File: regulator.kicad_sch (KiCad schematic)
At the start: 20 parts, among them U3 LMR51635, U4 INA180A2

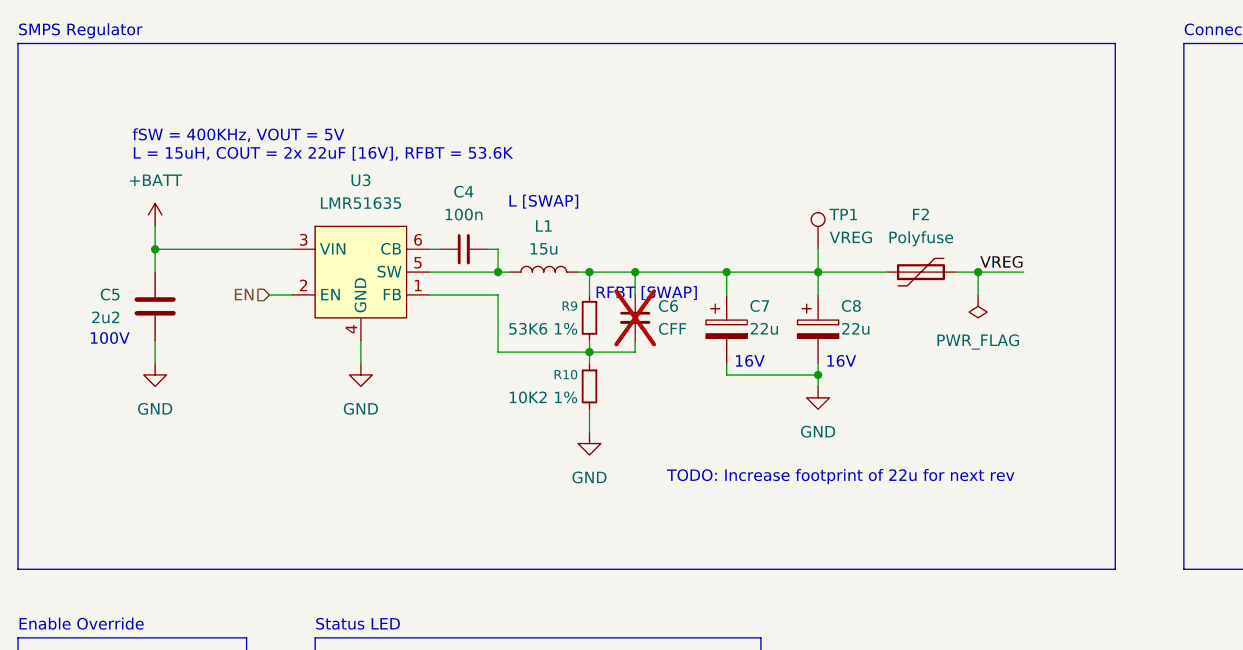
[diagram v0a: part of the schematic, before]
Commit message: fix capacitor sizes, clean up silkscreen, export
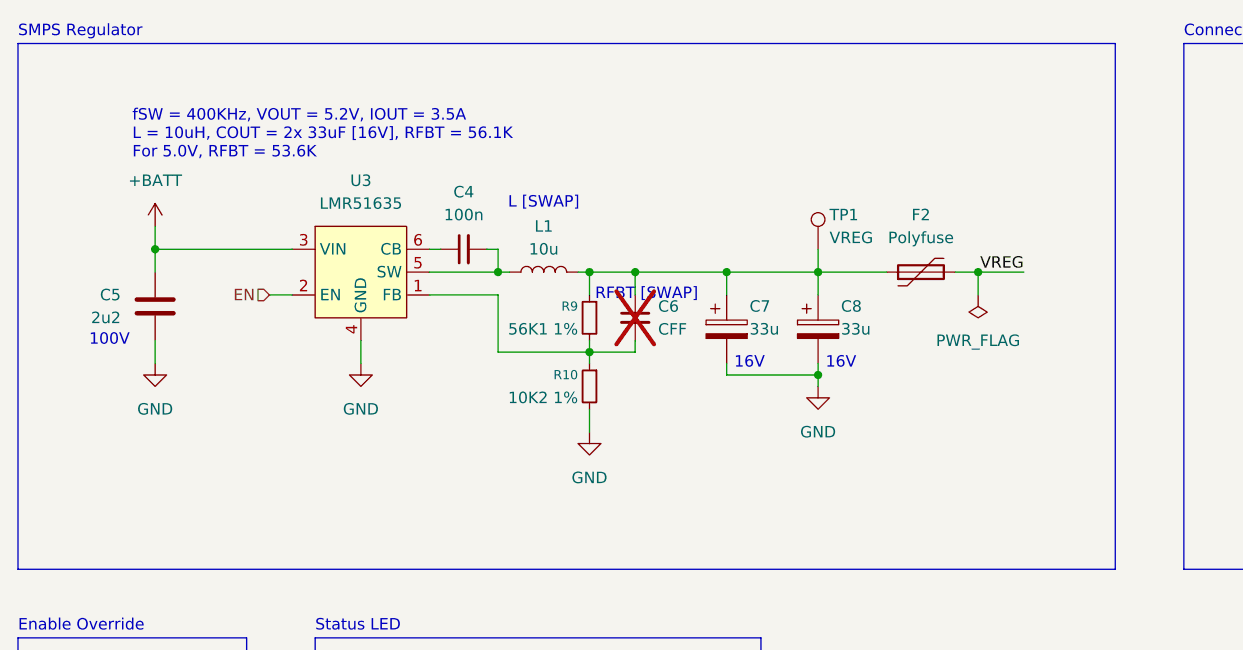
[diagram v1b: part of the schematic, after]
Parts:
- C7, C8: value 22u -> 33u; footprint Capacitor_SMD:C_0805_2012Metric -> Capacitor_Tantalum_SMD:CP_EIA-3528-12_Kemet-T
- L1: value 15u -> 10u
- R9: value 53K6 1% -> 56K1 1%
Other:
- note added: "fSW = 400KHz, VOUT = 5.2V, IOUT = 3.5A L = 10uH, COUT = 2x 33uF [16V], RFBT = 56.1K For 5.0V, RFBT = 53.6K"
- note removed: "TODO: Increase footprint of 22u for next rev"
- note removed: "fSW = 400KHz, VOUT = 5V L = 15uH, COUT = 2x 22uF [16V], RFBT = 53.6K"
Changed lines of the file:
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@@
 		)
 	)
-	(text "TODO: Increase footprint of 22u for next rev"
+	(text "fSW = 400KHz, VOUT = 5.2V, IOUT = 3.5A\nL = 10uH, COUT = 2x 33uF [16V], RFBT = 56.1K\nFor 5.0V, RFBT = 53.6K"
 		(exclude_from_sim no)
-		(at 109.22 67.31 0)
-		(effects
-			(font
-				(size 1.27 1.27)
-			)
-		)
-	)
-	(text "fSW = 400KHz, VOUT = 5V\nL = 15uH, COUT = 2x 22uF [16V], RFBT = 53.6K"
-		(exclude_from_sim no)
-		(at 30.48 30.48 0)
+		(at 30.48 29.21 0)
 		(effects
 			(font
@@
 			)
 		)
-		(property "Value" "22u"
+		(property "Value" "33u"
 			(at 99.06 50.8 0)
 			(effects
@@
 			)
 		)
-		(property "Footprint" "Capacitor_SMD:C_0805_2012Metric"
+		(property "Footprint" "Capacitor_Tantalum_SMD:CP_EIA-3528-12_Kemet-T"
 			(at 97.4852 54.61 0)
 			(effects
@@
 			)
 		)
-		(property "Value" "53K6 1%"
+		(property "Value" "56K1 1%"
 			(at 80.01 50.8 0)
 			(effects
@@
 			)
 		)
-		(property "Value" "15u"
+		(property "Value" "10u"
 			(at 76.2 41.91 90)
 			(effects
@@
 			)
 		)
-		(property "Value" "22u"
+		(property "Value" "33u"
 			(at 109.22 50.8 0)
 			(effects
@@
 			)
 		)
-		(property "Footprint" "Capacitor_SMD:C_0805_2012Metric"
+		(property "Footprint" "Capacitor_Tantalum_SMD:CP_EIA-3528-12_Kemet-T"
 			(at 107.6452 54.61 0)
 			(effects
